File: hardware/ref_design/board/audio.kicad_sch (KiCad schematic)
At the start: 7 parts, among them J4 SPEAKER, U7 MAX98357AETE+T

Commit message: Reference design: case, board pipeline, routing tools and docs
- case/case.scad now owns every position the board needs (outline,
  cable slot, contacts, screws, USB-C, power button, pinholes, light
  pipes, height limits) and exports them to positions.json; tub, lid
  and power cap STLs, lens and board outlines as DXF.
- board/placement.py + tools/build_pcb.py: a 4-layer board built from
  KiCad's netlist with pcbnew, every footprint linked to its symbol
  (DRC schematic parity: 0), the RP2350B core's placement, routing and
  regulator copper copied from Raspberry Pi's minimal design.
- tools/route.py: planes, pre-routes the autorouter can't do (membrane
  combs, the display's grounded RGB pins, plane fan-out), Freerouting
  1.9 on a corrected copy of the board, pours, stitching, repair.
- Footprint copies that carry vendor 3D models (USB-C, JST, switches)
  checked against their pads; speaker pads moved to the back as SMD;
  the Alps switch's pads pulled back from its locating holes.
- docs: README, assembly, bring-up, pin map (generated), BOM, design
  review, and the Konnect problems met on the way.

Co-Authored-By: Claude Opus 5.5 (1M context) <noreply@anthropic.com>
Claude-Session: https://claude.ai/code/session_01KGgEu3CbFtCsvHRQgAFiCN
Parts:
- J4: footprint Connector_Wire:SolderWire-0.15sqmm_1x02_P4mm_D0.5mm_OD1.5mm -> battler:Speaker_Wire_Pads_P4.0mm
- U7: footprint Package_DFN_QFN:TQFN-16-1EP_3x3mm_P0.5mm_EP1.23x1.23mm -> Package_DFN_QFN:TQFN-16-1EP_3x3mm_P0.5mm_EP1.23x1.23mm_ThermalVias
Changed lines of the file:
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@@
         (font
           (size 1.27 1.27))))
-    (property "Footprint" "Package_DFN_QFN:TQFN-16-1EP_3x3mm_P0.5mm_EP1.23x1.23mm"
+    (property "Footprint" "Package_DFN_QFN:TQFN-16-1EP_3x3mm_P0.5mm_EP1.23x1.23mm_ThermalVias"
       (at 55.88 45.72 0)
       (effects
@@
         (font
           (size 1.27 1.27))))
-    (property "Footprint" "Connector_Wire:SolderWire-0.15sqmm_1x02_P4mm_D0.5mm_OD1.5mm"
+    (property "Footprint" "battler:Speaker_Wire_Pads_P4.0mm"
       (at 226.06 27.94 0)
       (effects

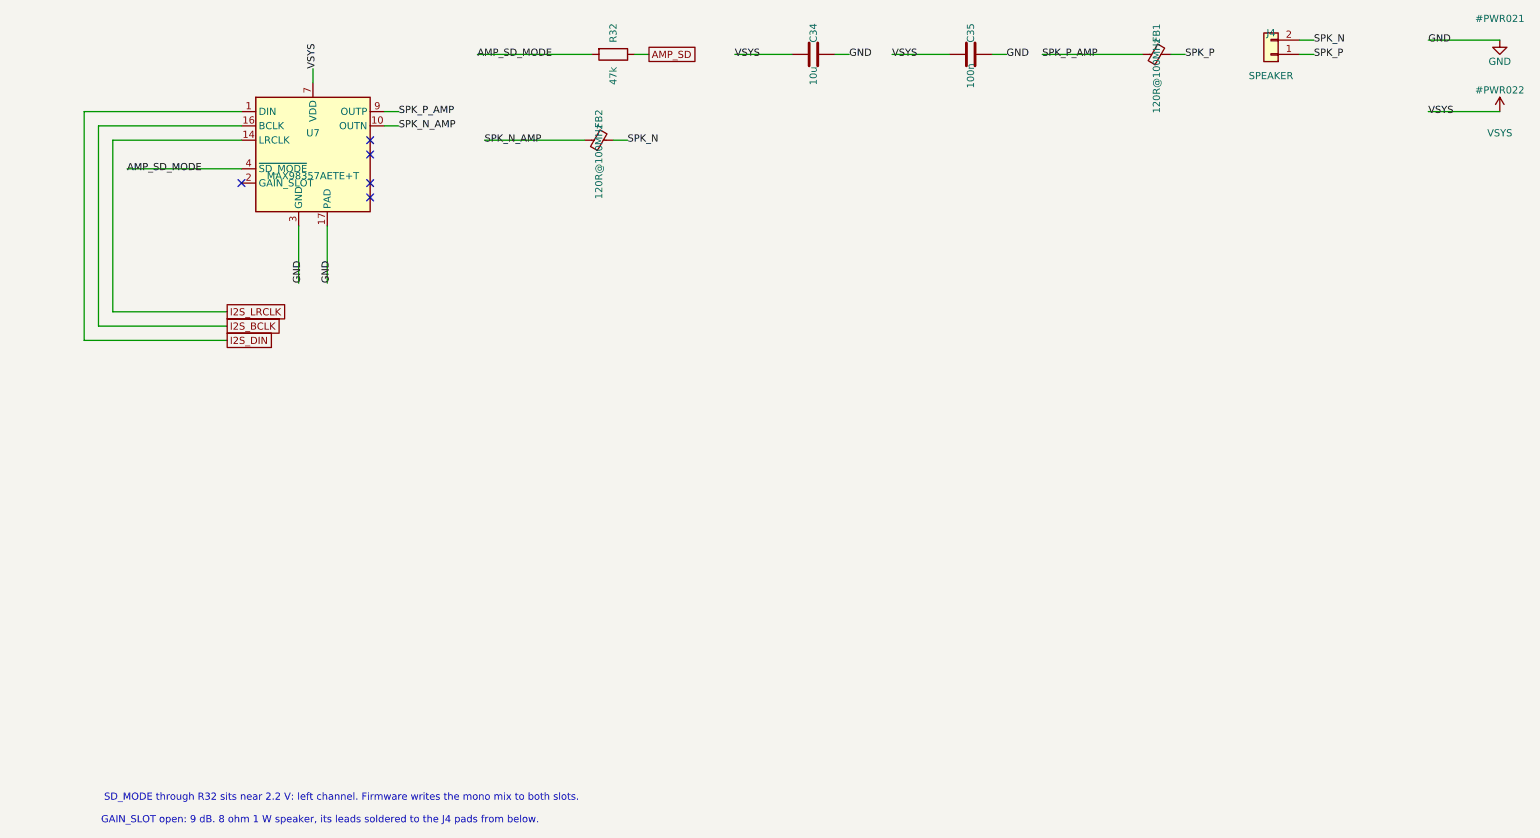
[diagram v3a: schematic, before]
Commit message: 2-layer fork: approved circuit changes in the design data and schematic
TP4056 charger (500 mA, TEMP grounded) with USB load sharing (B5819W, AO3401A
gate fed through a BAT54WS so it switches at once on an unplug, 22 uF on VSYS),
ME6211 3V3 LDO on the power latch, RP2354B with its flash inside (only the
QSPI_SS strap outside), 27 ohm 0603 USB resistors, SRV05-4 ESD, PWM audio
through two RC poles into an FM8002A, seat 1's Y contact as the power button,
no LEDs, no thermistor. Thermal-via footprints use 0.3 mm holes. Netlist
check passes, ERC 0 errors.

Co-Authored-By: Claude Opus 5.5 <noreply@anthropic.com>
Claude-Session: https://claude.ai/code/session_01KGgEu3CbFtCsvHRQgAFiCN
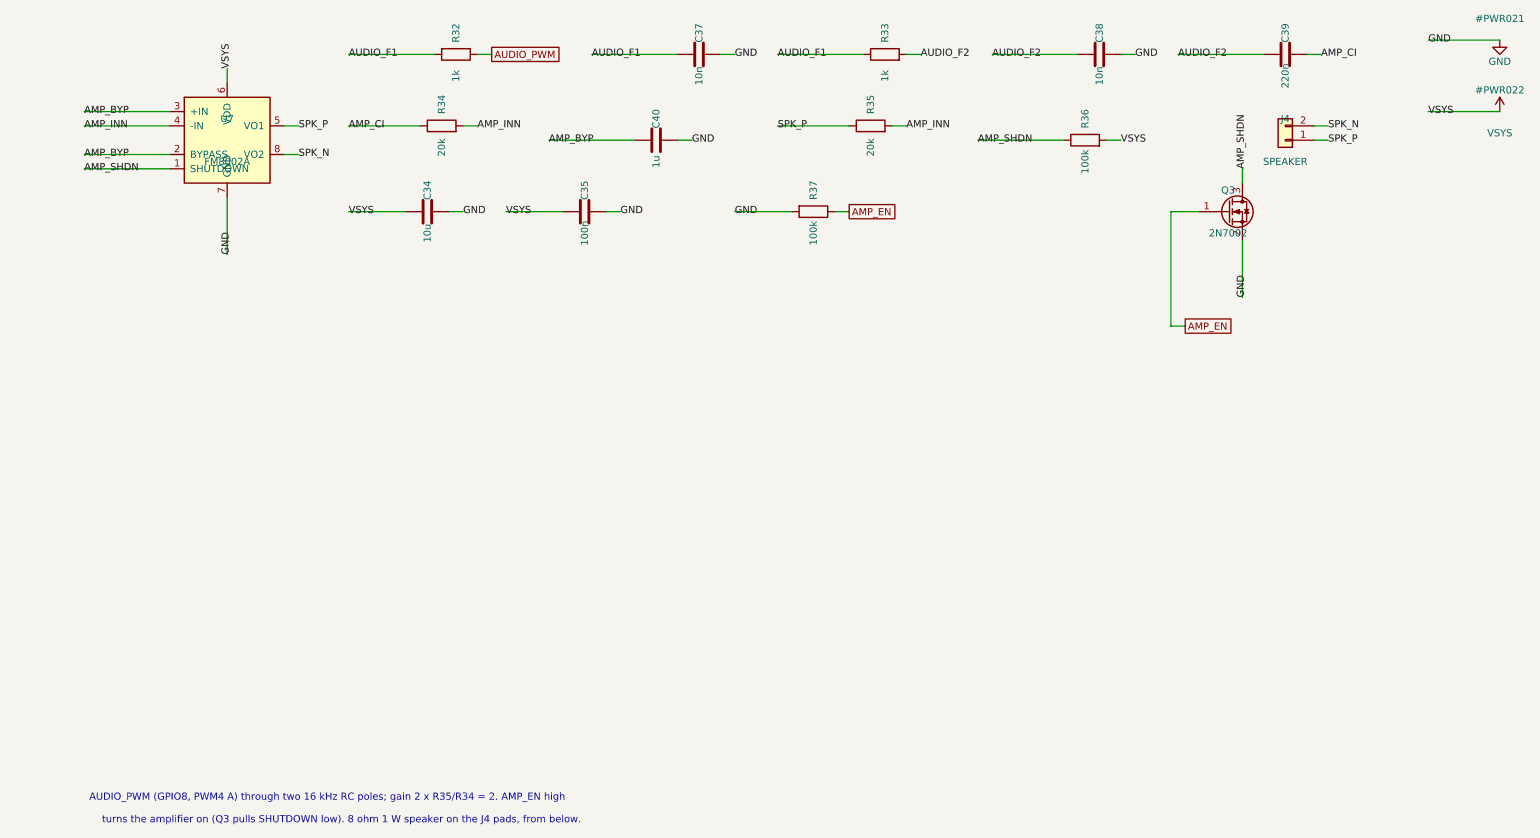
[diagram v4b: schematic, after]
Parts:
- removed FB1, FB2: 120R@100MHz, Inductor_SMD:L_0603_1608Metric, symbol Device:FerriteBead_Small
- removed U7: MAX98357AETE+T, Package_DFN_QFN:TQFN-16-1EP_3x3mm_P0.5mm_EP1.23x1.23mm_ThermalVias, symbol Audio:MAX98357A
- added C37, C38: 10n, Capacitor_SMD:C_0402_1005Metric, symbol Device:C
- added C39: 220n, Capacitor_SMD:C_0402_1005Metric, symbol Device:C
- added C40: 1u, Capacitor_SMD:C_0402_1005Metric, symbol Device:C
- added Q3: 2N7002, Package_TO_SOT_SMD:SOT-23, symbol Transistor_FET:Q_NMOS_GSD
- added R33: 1k, Resistor_SMD:R_0402_1005Metric, symbol Device:R
- added R34, R35: 20k, Resistor_SMD:R_0402_1005Metric, symbol Device:R
- added R36, R37: 100k, Resistor_SMD:R_0402_1005Metric, symbol Device:R
- added U7: FM8002A, Package_SO:SOIC-8_3.9x4.9mm_P1.27mm, symbol battler:FM8002A
- R32: value 47k -> 1k; LCSC C25792 -> C11702; MPN 0402WGF4702TCE -> 0402WGF1001TCE
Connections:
- net GND: now also C37.2, C38.2, C40.2, Q3.2 (S), R37.2, U7.7 (GND)
- net SPK_N: now also U7.8 (VO2)
- net SPK_P: now also R35.1, U7.5 (VO1)
- net VSYS: now also R36.2, U7.6 (VDD)
- net AMP_SD renamed AUDIO_PWM
- net AMP_SD_MODE renamed AUDIO_F1
- net AUDIO_F1: now also C37.1, R33.1
- new net AMP_BYP: C40.1, U7.2 (BYPASS), U7.3 (+IN)
- new net AMP_CI: C39.2, R34.1
- new net AMP_EN: Q3.1 (G), R37.1
- new net AMP_INN: R34.2, R35.2, U7.4 (-IN)
- new net AMP_SHDN: Q3.3 (D), R36.1, U7.1 (SHUTDOWN)
- new net AUDIO_F2: C38.1, C39.1, R33.2
- no-connect marks 5 -> 0
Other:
- note added: "AUDIO_PWM (GPIO8, PWM4 A) through two 16 kHz RC poles; gain 2 x R35/R34 = 2. AMP_EN high"
- note added: "turns the amplifier on (Q3 pulls SHUTDOWN low). 8 ohm 1 W speaker on the J4 pads, from below."
- note removed: "GAIN_SLOT open: 9 dB. 8 ohm 1 W speaker, its leads soldered to the J4 pads from below."
- note removed: "SD_MODE through R32 sits near 2.2 V: left channel. Firmware writes the mono mix to both slots."
